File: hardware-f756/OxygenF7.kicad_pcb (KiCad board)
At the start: 2 copper layers, 78 x 37 mm, 52 parts, among them J1 Conn_01x04, J10 Micro_SD_Card_Det, J2 USB_C_2.0, J3 JST SH-4, J4 JST ZH-4, J5 Conn_03x08, J6 Conn_01x16, J7 Conn_01x04, J9 JST GH-6, SW1 SW_Push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

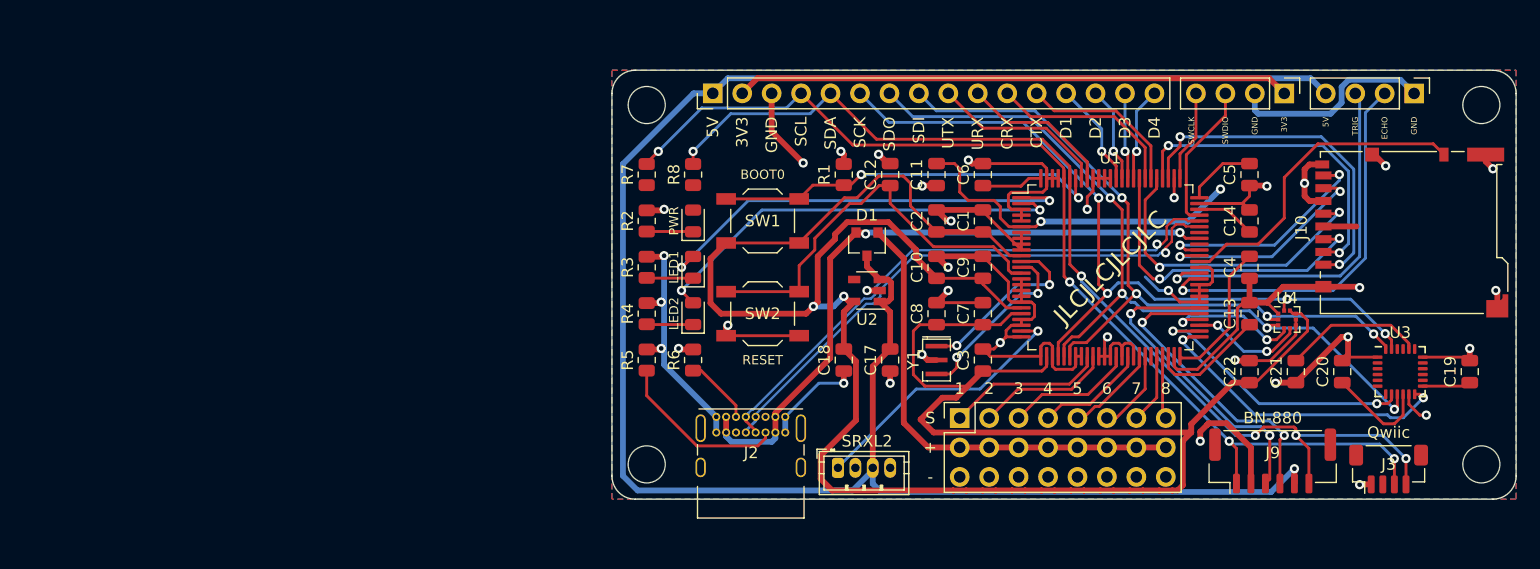
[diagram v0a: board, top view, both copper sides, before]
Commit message: Swap out some out-of-stock parts
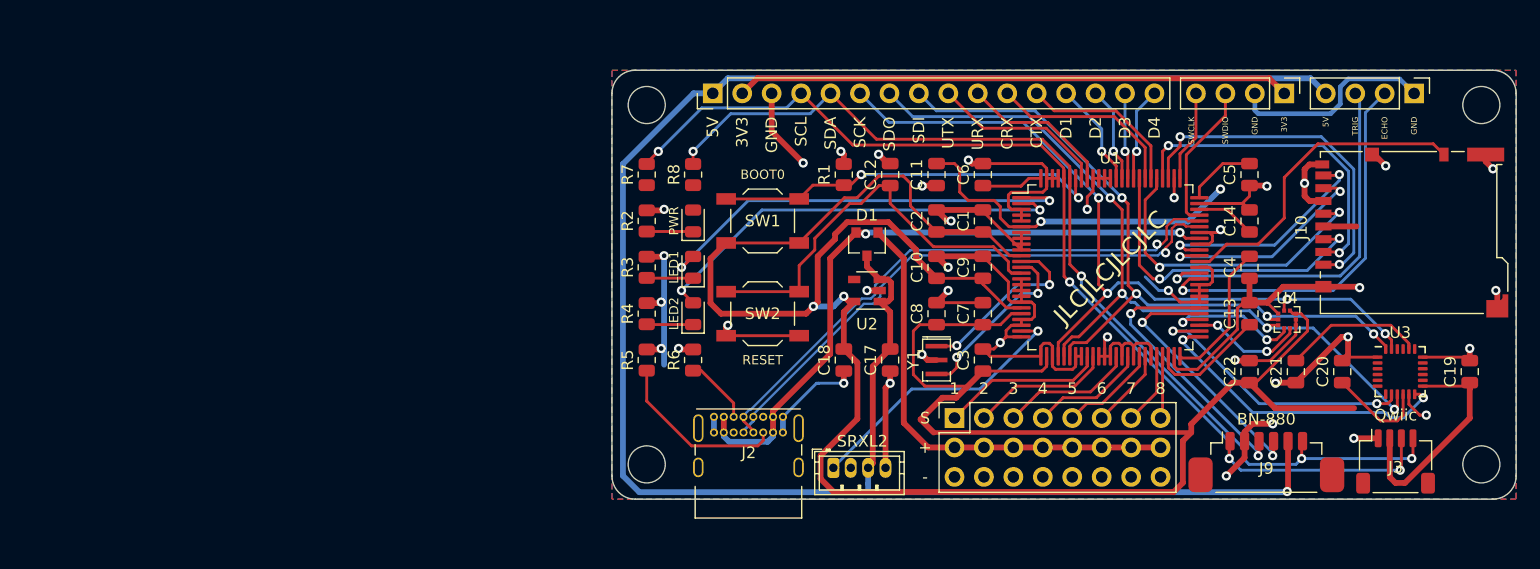
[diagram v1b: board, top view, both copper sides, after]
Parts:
- C17, C18: value 1u -> 10u
- J3: footprint Connector_JST:JST_SH_BM04B-SRSS-TB_1x04-1MP_P1.00mm_Vertical -> Connector_JST:JST_SH_SM04B-SRSS-TB_1x04-1MP_P1.00mm_Horizontal
- J9: value JST GH-6 -> 1.25mm; footprint Connector_JST:JST_GH_BM06B-GHS-TBT_1x06-1MP_P1.25mm_Vertical -> Sonrise:10114830-10106LF_P1.25mm_Horizontal
- U2: value AP2112K-3.3 -> XC6220B331MR
- moved J3 0.88 mm to (228.6, 115.8)
- moved J9 0.56 mm to (217.4, 115.8)
- moved J5 0.45 mm to (190.6, 112.0)
- moved J4 0.40 mm to (180.1, 116.3)
- moved J2 0.20 mm to (169.8, 111.9)
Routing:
- net +3V3: track 316.1 -> 342.4 mm
- net GND: track 252.1 -> 259.8 mm, vias 36 -> 38
- net USART3_TX: track 26.0 -> 22.7 mm
- net USART3_RX: track 27.3 -> 24.2 mm
- net I2C1_SCL: track 90.7 -> 87.9 mm, vias 5 -> 4
- net +5V: track 175.7 -> 177.1 mm

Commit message: New board layout
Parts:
- added C15: 0.1u, Capacitor_SMD:C_0805_2012Metric, F.Cu at (180.1, 114.0)
- added R10: 47k, Resistor_SMD:R_0805_2012Metric, F.Cu at (158.0, 88.0)
- added R11: 47k, Resistor_SMD:R_0805_2012Metric, F.Cu at (166.0, 88.0)
- added R12: 47k, Resistor_SMD:R_0805_2012Metric, F.Cu at (162.0, 88.0)
- added R13: 47k, Resistor_SMD:R_0805_2012Metric, F.Cu at (166.0, 92.0)
- added R14: 47k, Resistor_SMD:R_0805_2012Metric, F.Cu at (166.0, 96.0)
- added R15: 47k, Resistor_SMD:R_0805_2012Metric, F.Cu at (166.0, 100.0)
- added R16: 100k, Resistor_SMD:R_0805_2012Metric, F.Cu at (150.0, 110.0)
- added R17: 10k, Resistor_SMD:R_0805_2012Metric, F.Cu at (162.0, 108.0)
- added R18: 10k, Resistor_SMD:R_0805_2012Metric, F.Cu at (162.0, 104.0)
- added R19: 10k, Resistor_SMD:R_0805_2012Metric, F.Cu at (154.0, 88.0)
- added R9: 10k, Resistor_SMD:R_0805_2012Metric, F.Cu at (162.0, 100.0)
- added U5: W25Q128JVS, Package_SO:SOIC-8_5.23x5.23mm_P1.27mm, F.Cu at (180.0, 107.0)
- moved J1 105.2 mm to (116.0, 105.5), turned to 0 degrees
- moved J3 95.7 mm to (133.0, 119.8)
- moved C13 62.4 mm to (154.0, 110.0), turned to 90 degrees
- moved C20 62.1 mm to (162.0, 112.0)
- moved C19 61.1 mm to (174.0, 112.0)
- moved U3 61.1 mm to (168.0, 111.0)
- moved C4 59.0 mm to (158.0, 110.0), turned to 90 degrees
- moved D1 58.0 mm to (127.0, 112.0), turned to 90 degrees
- moved J4 57.6 mm to (122.6, 120.3)
- moved U2 56.4 mm to (127.0, 108.0), turned to 0 degrees
- moved J2 55.3 mm to (119.0, 90.0), turned to 270 degrees
- moved C14 54.0 mm to (162.0, 96.0), turned to 270 degrees
- moved C5 54.0 mm to (162.0, 92.0)
- moved C17 53.2 mm to (132.0, 112.0)
- moved J7 53.2 mm to (177.2, 80.0)
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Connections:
- D1 pad 1: +5V_BEC -> VBUS
- D1 pad 2: VBUS -> +5V_BEC
- J6 pad 10: USART1_TX -> SPI1_MOSI
- J6 pad 11: CAN1_TX -> GPIO_1
- J6 pad 12: CAN1_RX -> GPIO_2
- J6 pad 13: GPIO_1 -> GPIO_3
- J6 pad 14: GPIO_2 -> GPIO_4
- J6 pad 15: GPIO_3 -> CAN1_TX
- J6 pad 16: GPIO_4 -> CAN1_RX
- J6 pad 4: I2C1_SDA -> UART8_TX
- J6 pad 5: I2C1_SCL -> UART8_RX
- J6 pad 6: SPI1_SCLK -> I2C1_SDA
- J6 pad 7: SPI1_MISO -> I2C1_SCL
- J6 pad 8: SPI1_MOSI -> SPI1_SCLK
- J6 pad 9: USART1_RX -> SPI1_MISO
- U1 pad 1: LED1 -> QUADSPI_IO2
- U1 pad 15: GND -> (no net)
- U1 pad 16: GND -> (no net)
- U1 pad 17: GND -> (no net)
- U1 pad 18: GND -> (no net)
- U1 pad 2: LED2 -> LED1
- U1 pad 22: GND -> (no net)
- U1 pad 23: GND -> (no net)
- U1 pad 25: GND -> (no net)
- U1 pad 28: GND -> (no net)
- U1 pad 3: GND -> LED2
- U1 pad 32: GND -> (no net)
- U1 pad 33: GND -> (no net)
- U1 pad 36: GND -> QUADSPI_SCLK
- U1 pad 37: GND -> (no net)
- U1 pad 38: GND -> (no net)
- U1 pad 4: GND -> (no net)
- U1 pad 40: GND -> (no net)
- U1 pad 42: GND -> (no net)
- U1 pad 45: GND -> (no net)
- U1 pad 5: GND -> (no net)
- U1 pad 57: GND -> (no net)
- U1 pad 58: GND -> QUADSPI_IO0
- U1 pad 59: GND -> QUADSPI_IO1
- U1 pad 60: GND -> QUADSPI_IO3
- U1 pad 61: ULTRA_ECHO -> (no net)
- U1 pad 62: ULTRA_TRIG -> (no net)
- U1 pad 63: GND -> (no net)
- U1 pad 67: GND -> ULTRA_ECHO
- U1 pad 69: GND -> ULTRA_TRIG
- U1 pad 7: GND -> (no net)
- U1 pad 77: GND -> (no net)
- U1 pad 8: GND -> (no net)
- U1 pad 84: GPIO_4 -> (no net)
- U1 pad 85: GPIO_3 -> (no net)
- U1 pad 86: GPIO_2 -> GPIO_4
- U1 pad 87: GPIO_1 -> GPIO_3
- U1 pad 88: GND -> GPIO_2
- U1 pad 89: GND -> GPIO_1
- U1 pad 9: GND -> (no net)
- U1 pad 90: GND -> (no net)
- U1 pad 91: GND -> (no net)
- U1 pad 92: USART1_TX -> QUADSPI_CS
- U1 pad 93: USART1_RX -> (no net)
- U1 pad 97: GND -> UART8_RX
- U1 pad 98: GND -> UART8_TX
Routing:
- net GND: track 259.8 -> 512.7 mm, vias 38 -> 36
- net QUADSPI_IO2: track 0.00 -> 63.9 mm, vias 0 -> 2
- net +3V3: track 342.4 -> 401.1 mm, vias 4 -> 6
- net SWCLK: track 7.90 -> 58.1 mm, vias 0 -> 1
- net QUADSPI_CS: track 0.00 -> 49.5 mm, vias 0 -> 3
- net SWDIO: track 12.9 -> 57.7 mm, vias 0 -> 1
- net QUADSPI_SCLK: track 0.00 -> 42.3 mm, vias 0 -> 2
- net QUADSPI_IO3: track 0.00 -> 28.8 mm, vias 0 -> 2
- net +5V: track 177.1 -> 205.5 mm, vias 1 -> 0
- net QUADSPI_IO1: track 0.00 -> 27.8 mm, vias 0 -> 2
- net QUADSPI_IO0: track 0.00 -> 26.4 mm, vias 0 -> 2
- net Net-(D2-Pad1): track 4.01 -> 27.3 mm
- net UART8_RX: track 0.00 -> 21.8 mm, vias 0 -> 1
- net UART8_TX: track 0.00 -> 21.1 mm, vias 0 -> 1
- net Net-(D3-Pad1): track 4.01 -> 20.0 mm
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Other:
- board size 78 x 37 mm -> 73 x 45 mm
- board text added: "Rev A @ 2021-05"
- board text removed: "Rev A @ 2021-04"
